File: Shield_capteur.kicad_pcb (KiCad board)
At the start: 2 copper layers, 79.2 x 66.2 mm, 24 parts, among them J1 Power, J2 Digital/PWM, J3 Analog, J4 Digital/PWM, K63 1uF, U1 LTC1050ACN8_PBF, U2 MCP

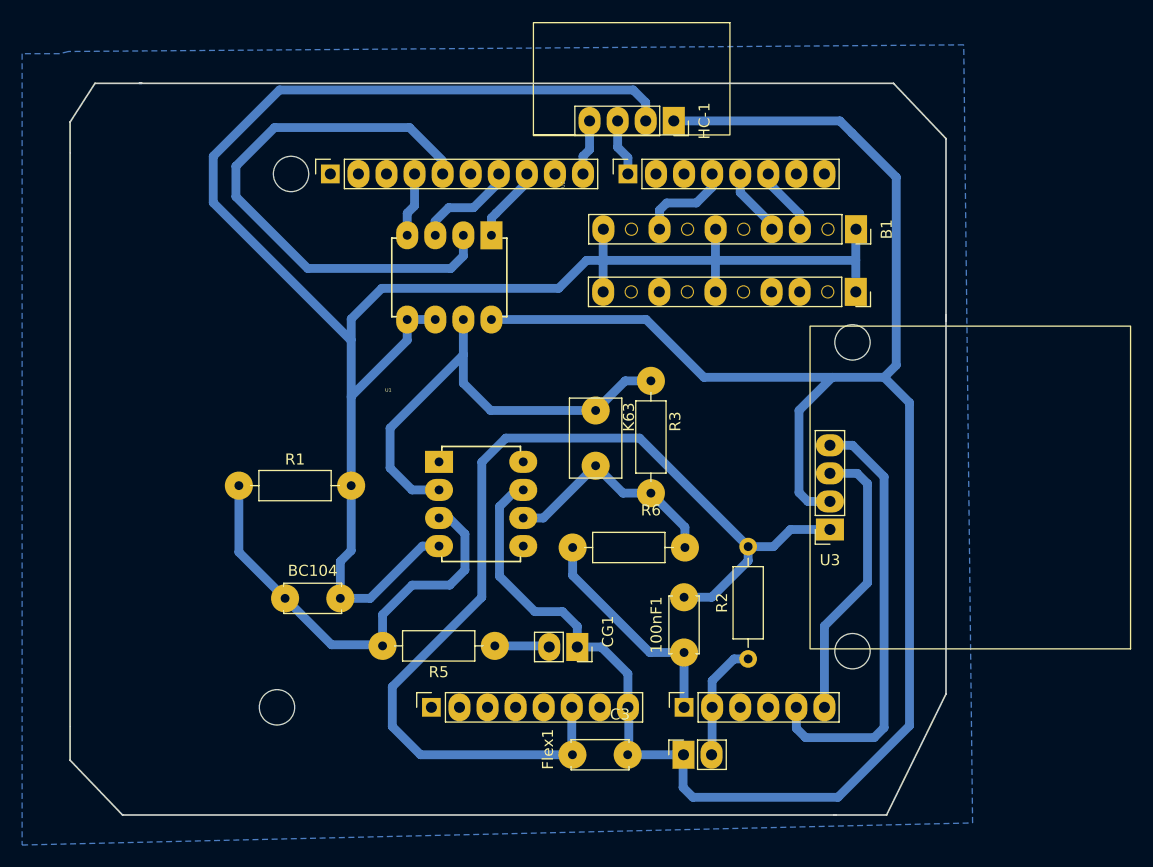
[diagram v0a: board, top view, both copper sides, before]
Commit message: Ajout lien second Arduino
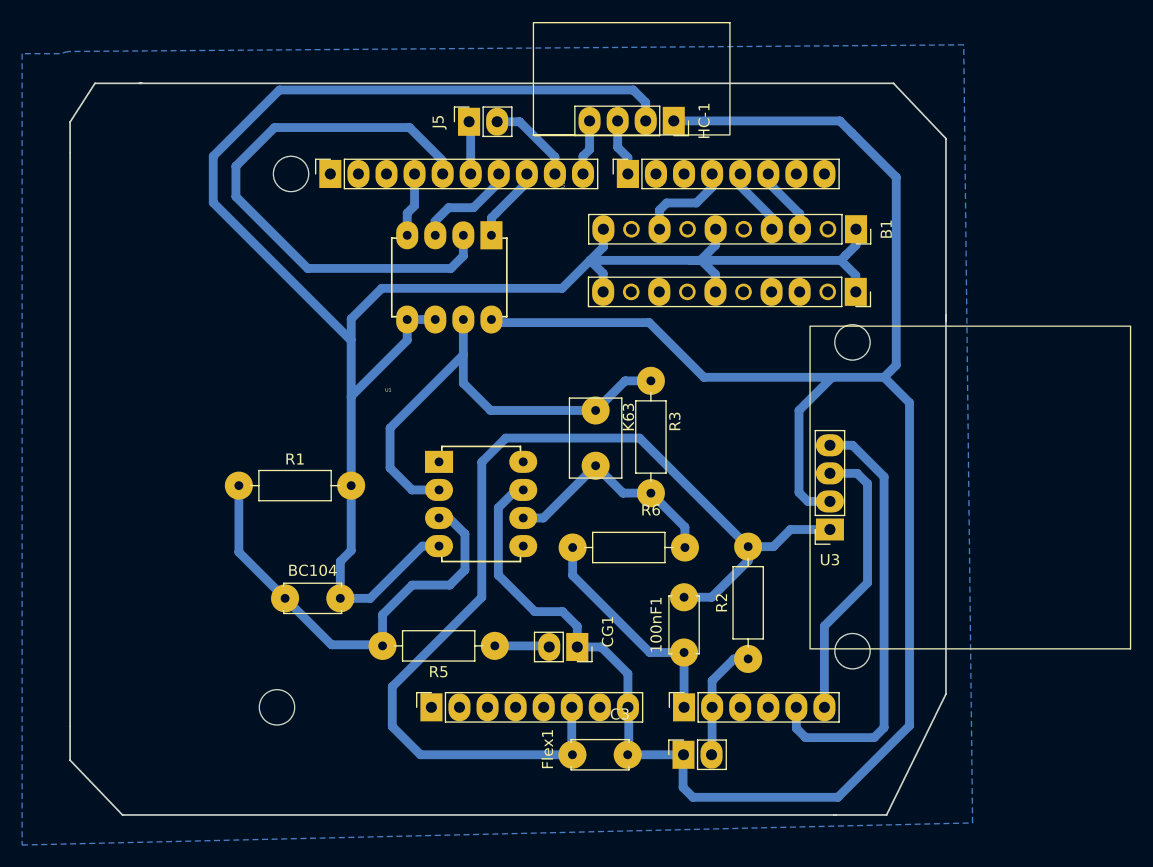
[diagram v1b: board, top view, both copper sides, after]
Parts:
- added J5: Conn_01x02_Pin, Connector_PinSocket_2.54mm:PinSocket_1x02_P2.54mm_Vertical, F.Cu at (131.3, 44.5)
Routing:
- net /D9: track 0.00 -> 8.08 mm
- net /D12: track 0.00 -> 4.79 mm
- net GND: track 280.5 -> 283.4 mm

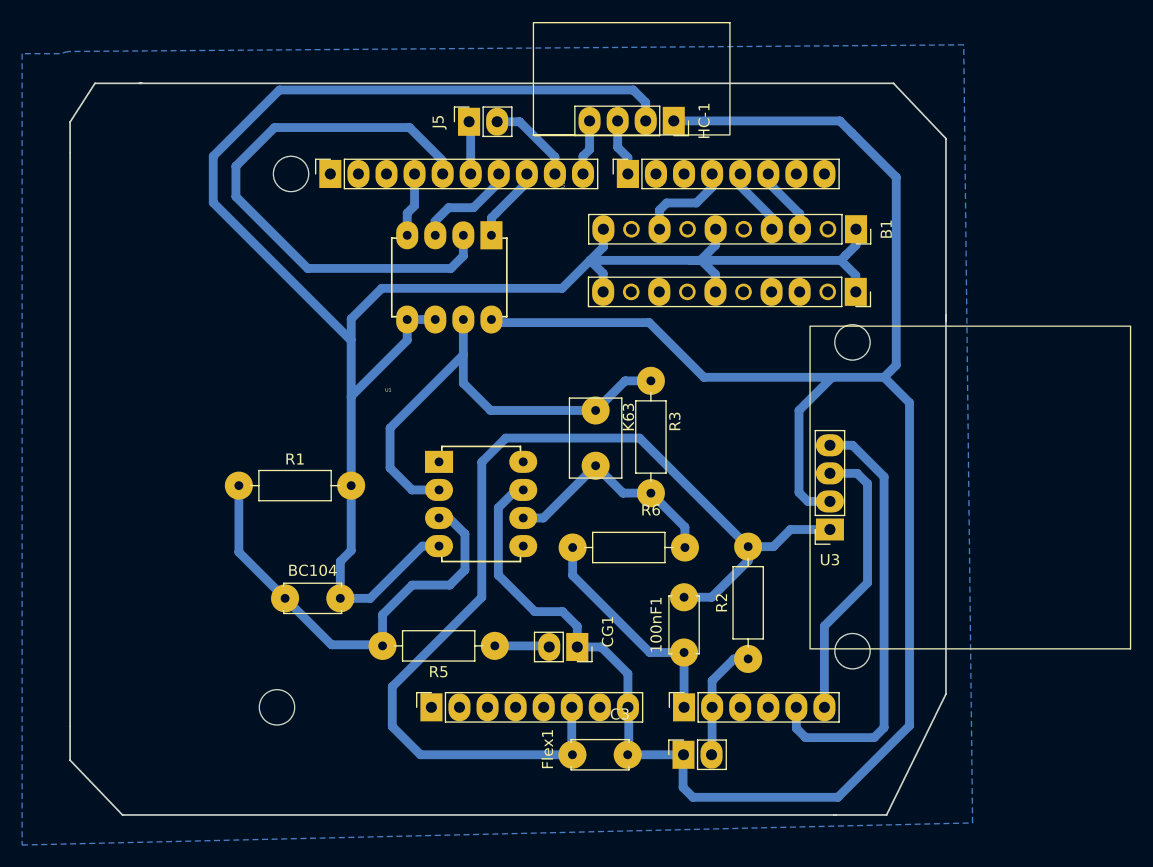
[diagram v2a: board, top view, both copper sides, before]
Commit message: Mise en forme shematic et rajout valeurs MCP
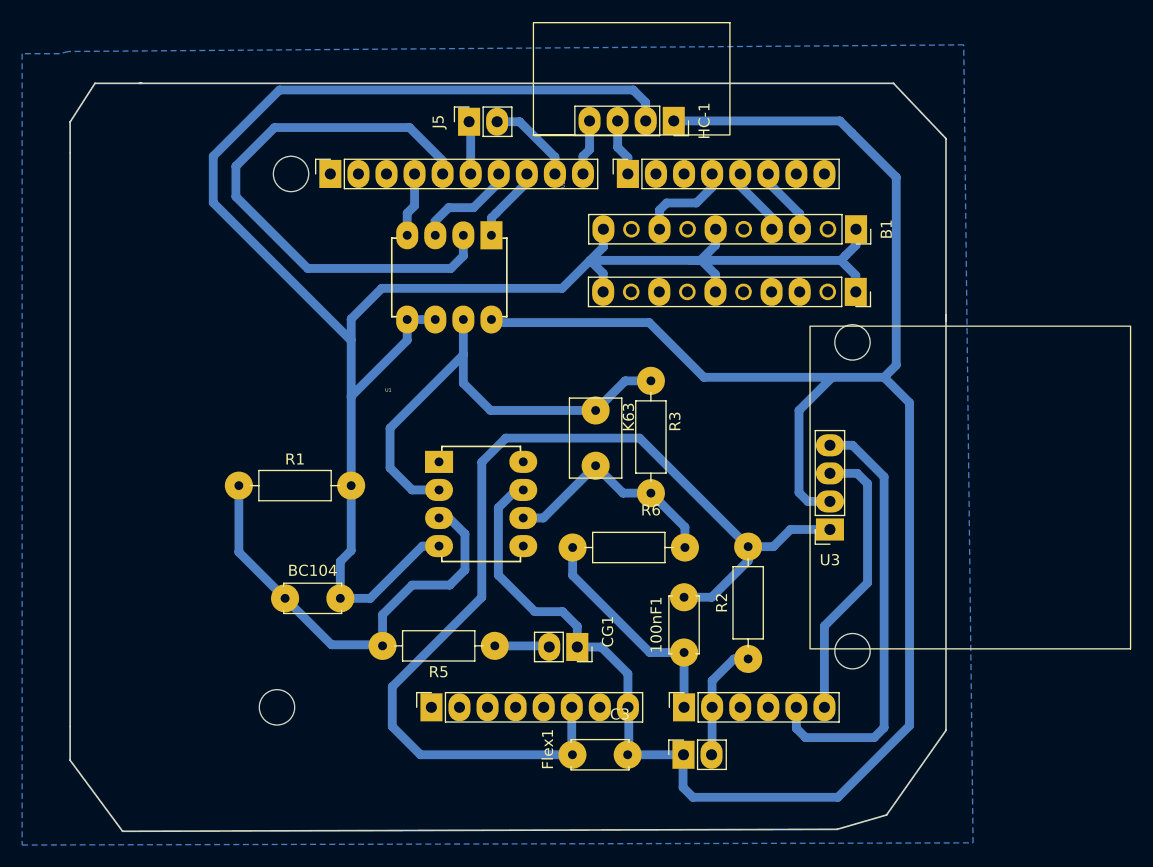
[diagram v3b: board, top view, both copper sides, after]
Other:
- board size 79.2 x 66.2 mm -> 79.2 x 67.7 mm
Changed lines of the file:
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@@
 	(gr_line
 		(start 169.125 107.2)
-		(end 174.5 96.25)
+		(end 174.5 99.55)
 		(stroke
 			(width 0.15)
@@
 	(gr_line
 		(start 174.5 61.96)
-		(end 174.5 96.25)
+		(end 174.5 99.55)
 		(stroke
 			(width 0.15)
@@
 	)
 	(gr_line
-		(start 164.508 107.2)
-		(end 99.992 107.2)
+		(start 164.65 108.5)
+		(end 100 108.675)
 		(stroke
 			(width 0.15)
@@
 	)
 	(gr_line
-		(start 99.992 107.2)
+		(start 100 108.675)
 		(end 95.25 102.25)
 		(stroke
@@
 	)
 	(gr_line
-		(start 164.375 107.2)
+		(start 164.65 108.5)
 		(end 169.125 107.2)
 		(stroke
@@
 		(polygon
 			(pts
-				(xy 90.905901 38.319251) (xy 90.905901 109.919251) (xy 176.905901 107.919251) (xy 176.105901 37.519251)
+				(xy 90.905901 38.319251) (xy 90.905901 109.919251) (xy 176.95 109.725) (xy 176.105901 37.519251)
 				(xy 95.105901 38.119251) (xy 94.305901 38.319251)
 			)
